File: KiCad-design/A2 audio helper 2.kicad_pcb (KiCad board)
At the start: 2 copper layers, 52 x 70 mm, 34 parts, among them J1 PIN HEADER 1x2, J10 PIN HEADER 1x4, J11 PIN HEADER 1x3, J12 PIN HEADER 1x3, J13 PIN HEADER 1x3, J2 PIN HEADER 1x2, J3 PIN HEADER 1x2, J4 PIN HEADER 1x2, J5 SJ1-3515N, J6 PIN HEADER 1x3, J7 PIN HEADER 1x3, J8 SJ1-3515N, J9 PIN HEADER 1x5, K1 SR11-5V-200-2C, SW2 SW_DPDT_x2, U1 pam8403

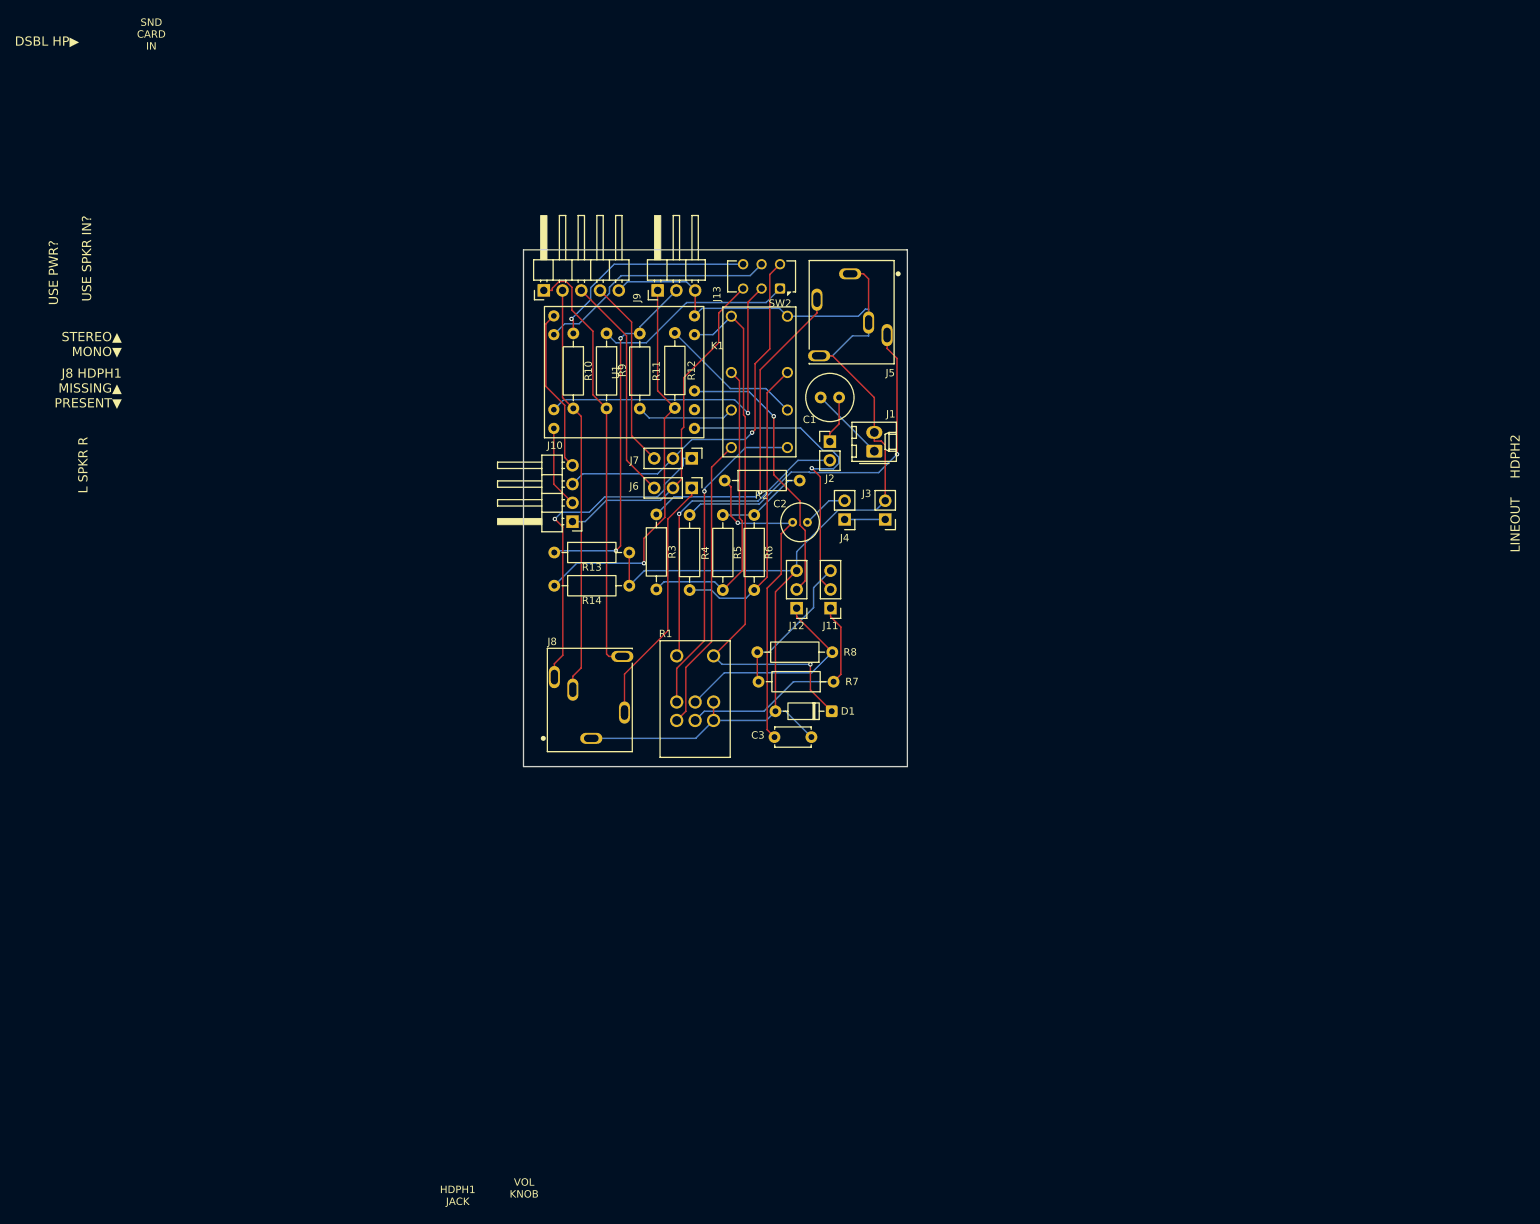
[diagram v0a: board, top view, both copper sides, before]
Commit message: minor simplification, 1st draft pcb
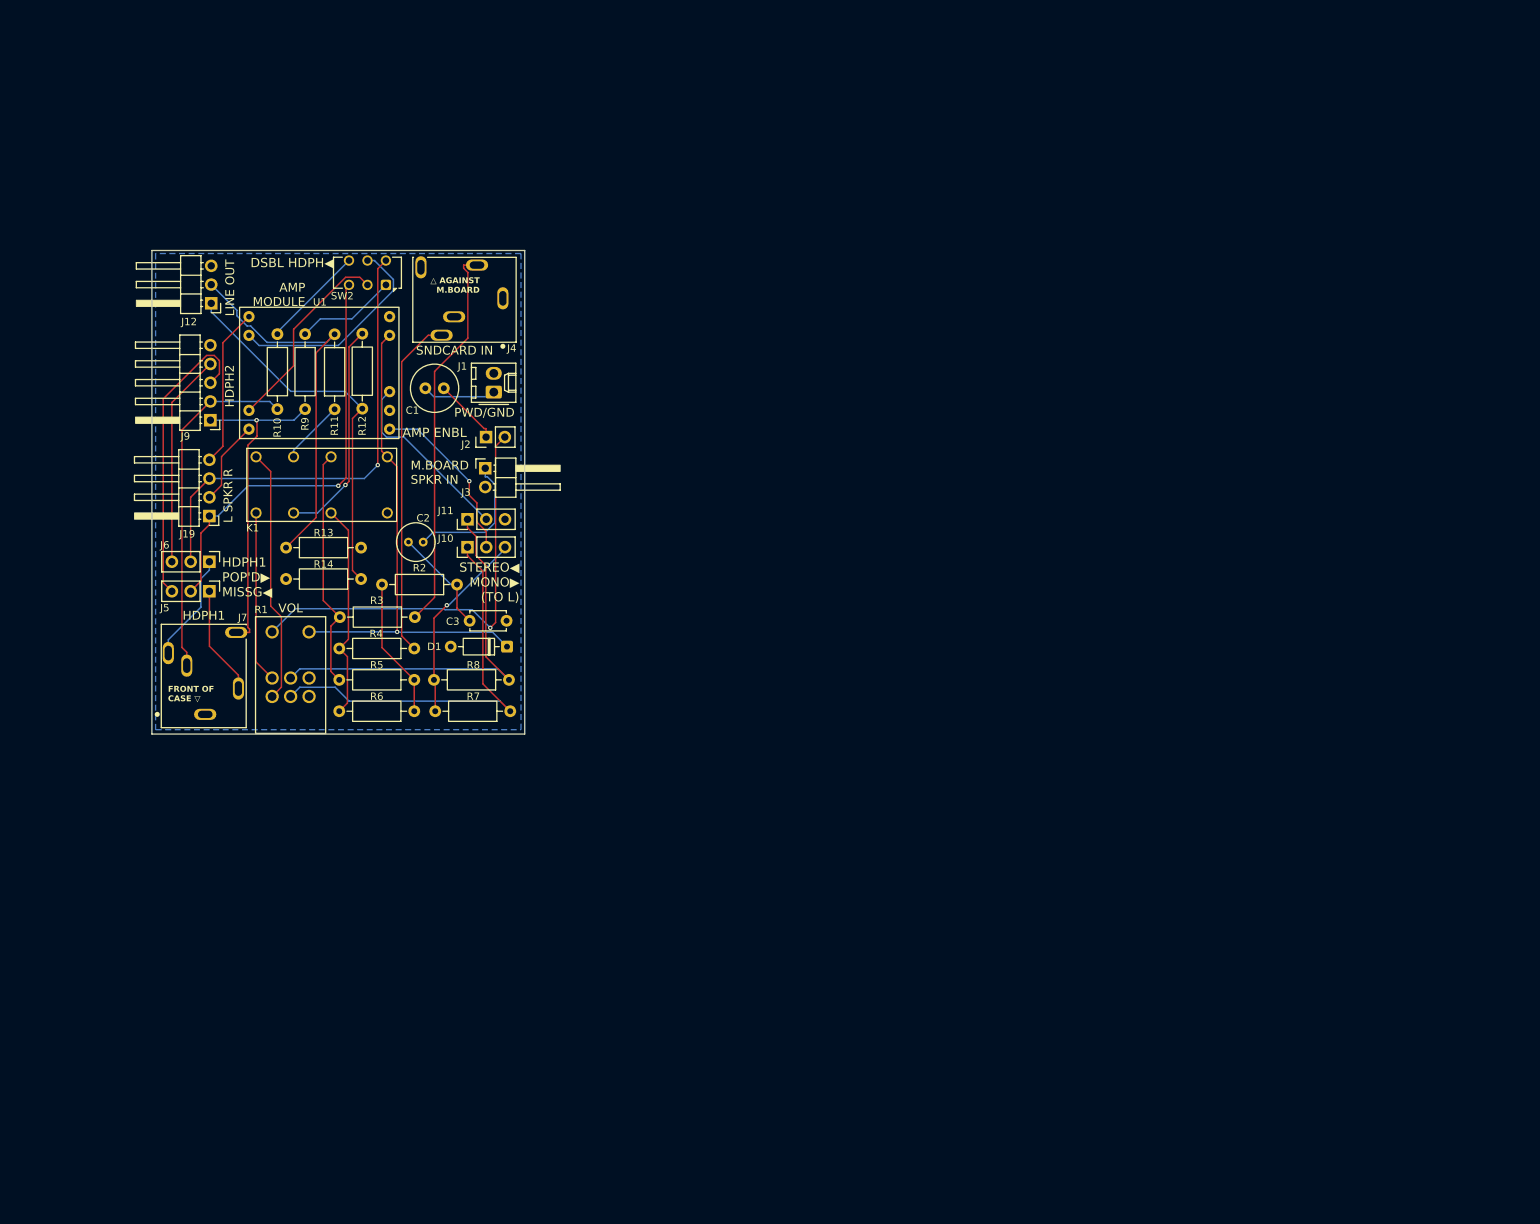
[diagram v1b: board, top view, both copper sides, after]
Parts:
- removed the J4 at (143.9, 86.5)
- J3: footprint Connector_PinHeader_2.54mm:PinHeader_1x02_P2.54mm_Vertical -> Connector_PinHeader_2.54mm:PinHeader_1x02_P2.54mm_Horizontal
- SW2: footprint Button_Switch_THT:SW_CK_JS202011AQN_DPDT_Angled -> Button_Switch_THT:SW_CK_JS202011CQN_DPDT_Straight
- moved J5 66.8 mm to (57.9, 96.2)
- moved J6 66.8 mm to (57.9, 92.2)
- moved K1 60.9 mm to (73.1, 81.8), turned to 0 degrees
- moved J12 60.5 mm to (58.1, 57.2), turned to 180 degrees
- moved R1 54.9 mm to (68.9, 108.0)
- moved J3 54.6 mm to (95.2, 79.6), turned to 0 degrees
- moved C1 53.6 mm to (87.1, 68.8)
- moved SW2 53.4 mm to (81.8, 54.8)
- moved R6 53.2 mm to (85.6, 112.5), turned to 180 degrees
- moved J7 52.4 mm to (57.3, 112.9)
- moved J1 52.2 mm to (96.4, 69.3)
- moved C2 52.1 mm to (86.8, 89.6)
- moved J10 49.9 mm to (92.8, 90.3), turned to 90 degrees
- moved J19 49.2 mm to (57.9, 86.1)
- moved J9 48.5 mm to (58.0, 73.1), turned to 180 degrees
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- renumbered J11 to J10, J12 to J11, J13 to J12, J10 to J19, J5 to J4, J6 to J5, J7 to J6, J8 to J7
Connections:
- C2 pad 1: Net-(J4-Pin_2) -> /MB_SPKR
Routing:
- net GND: track 185.7 -> 0.00 mm
- net /HP1_IS_PRIMARY_R: track 45.3 -> 14.7 mm, vias 1 -> 0
- net Net-(C2-Pad2): track 44.9 -> 14.6 mm, vias 1 -> 0
- net /VOLUME_ADJUSTED_R: track 29.3 -> 54.8 mm
- net /VOLUME_ADJUSTED_L: track 31.9 -> 56.2 mm
- net /VOLUME_SOURCE_R: track 44.0 -> 23.3 mm, vias 1 -> 0
- net /AMP_INPUT_L: track 43.5 -> 23.6 mm
- net /HP1_IS_PRIMARY_L: track 34.3 -> 14.8 mm
- net Net-(SW2A-B): track 45.2 -> 26.8 mm, vias 1 -> 0
- net /V_IN_ENABLED: track 42.8 -> 58.6 mm
- net Net-(SW2B-A): track 29.3 -> 14.0 mm, vias 1 -> 0
- net /HP_OUT_L: track 58.7 -> 44.6 mm, vias 0 -> 1
- net /MB_SPKR: track 5.50 -> 18.9 mm
- net Net-(SW2A-A): track 27.1 -> 13.7 mm
- net /AMP_INPUT_R: track 37.9 -> 25.0 mm, vias 1 -> 0
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- added copper zone on B.Cu, net GND
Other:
- board size 52 x 70 mm -> 50.5 x 65.5 mm
- board text added: "A2 Audio Helper v0.6"
- board text added: "AMP ENBL"
- board text added: "AMP MODULE"
- board text added: "DSBL HDPH◀︎"
- board text added: "FRONT OF CASE ▽"
- board text added: "HDPH1"
- board text added: "HDPH1 POP'D▶︎ MISSG◀︎"
- board text added: "LINE OUT"
- board text added: "M.BOARD SPKR IN"
- board text added: "Northwest Retroventures"
- board text added: "PWD/GND"
- board text added: "SNDCARD IN"
- board text added: "STEREO◀︎ MONO▶︎ (TO L)"
- board text added: "VOL"
- board text added: "△ AGAINST M.BOARD"
- board text removed: "DSBL HP▶︎"
- board text removed: "HDPH1 JACK"
- board text removed: "J8 HDPH1 MISSING▲ PRESENT▼"
- board text removed: "LINEOUT"
- board text removed: "SND CARD IN"
- board text removed: "STEREO▲ MONO▼"
- board text removed: "USE PWR?"
- board text removed: "USE SPKR IN?"
- board text removed: "VOL KNOB"

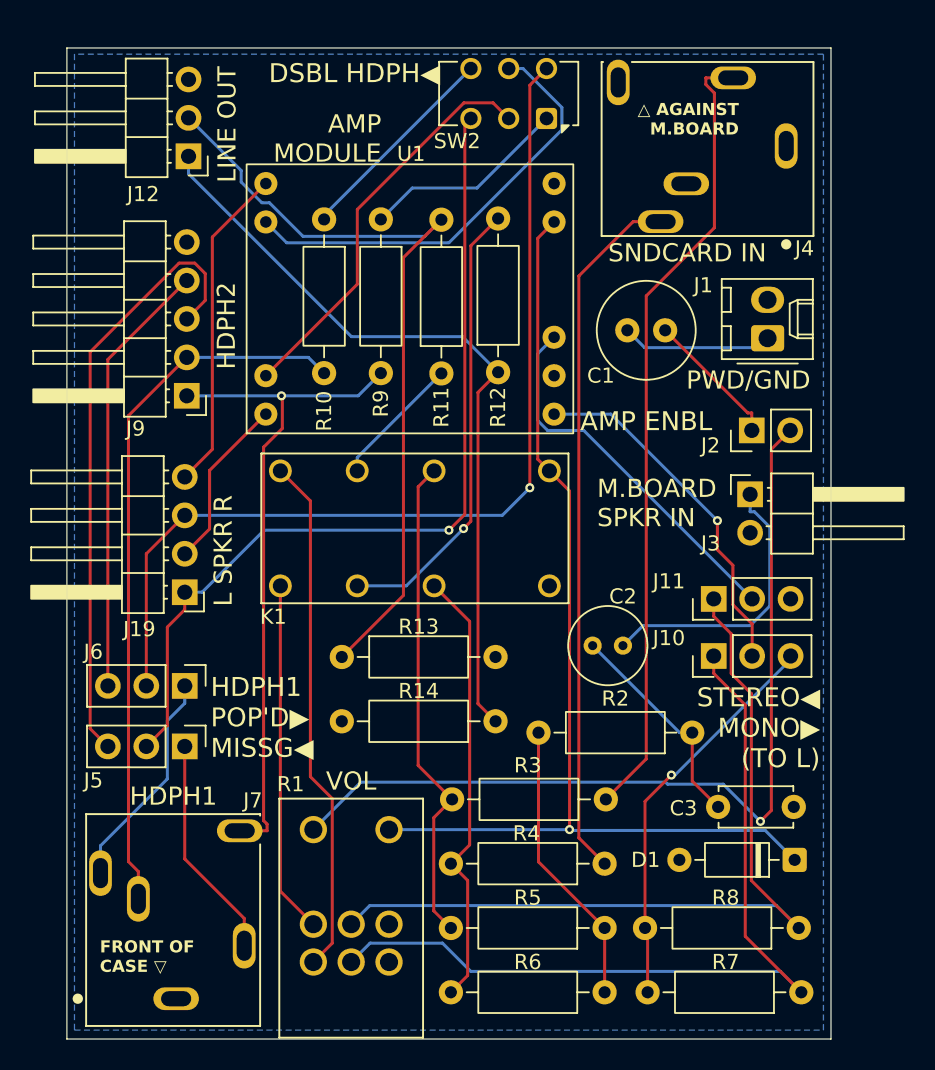
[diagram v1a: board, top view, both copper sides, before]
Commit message: picked new connectors, pcb take 2
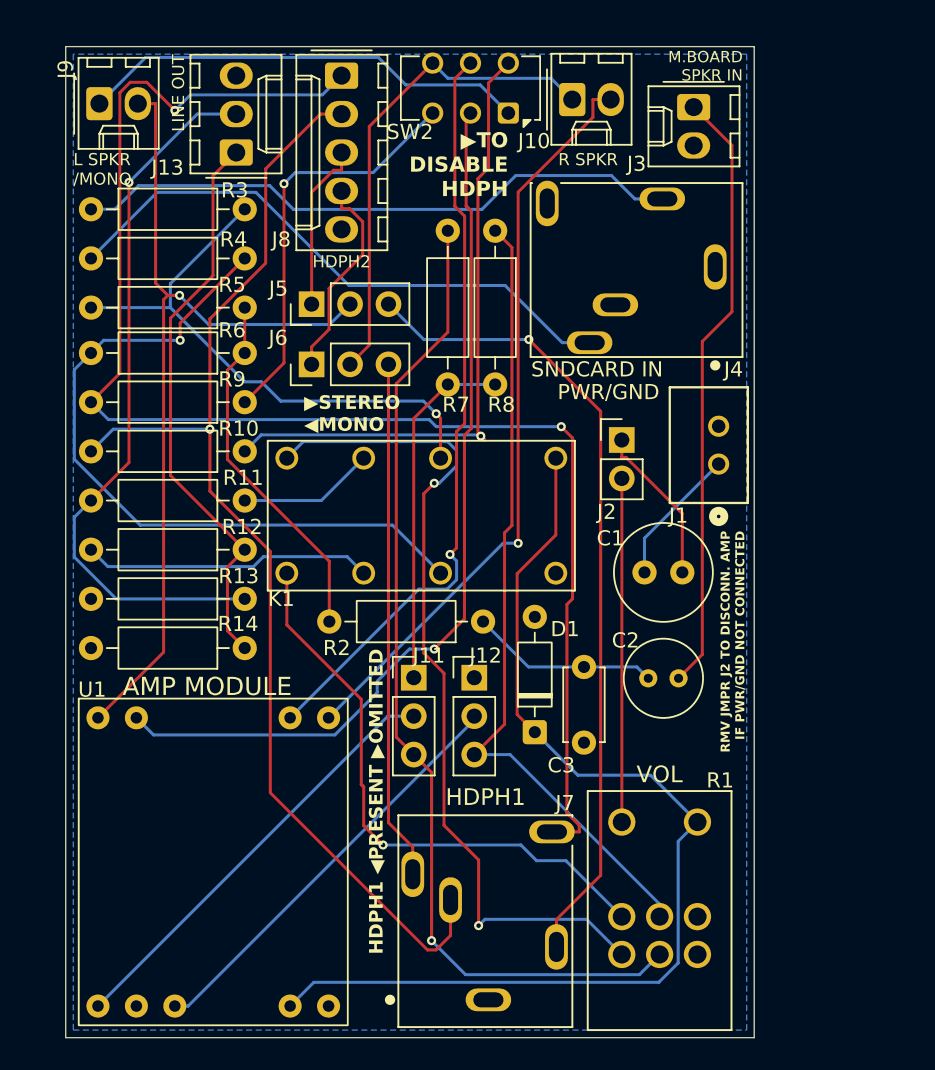
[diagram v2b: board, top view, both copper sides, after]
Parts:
- removed J19: PIN HEADER 1x4, Connector_PinHeader_2.54mm:PinHeader_1x04_P2.54mm_Horizontal
- added J10: PIN HEADER 1x2, Connector_Molex:Molex_KK-254_AE-6410-02A_1x02_P2.54mm_Vertical, F.Cu at (83.5, 53.5)
- added J9: PIN HEADER 1x2, Connector_Molex:Molex_KK-254_AE-6410-02A_1x02_P2.54mm_Vertical, F.Cu at (52.2, 53.8)
- J1: footprint Connector_Molex:Molex_KK-254_AE-6410-02A_1x02_P2.54mm_Vertical -> footprints:CONN_22035025_MOL
- J13: renamed from J12; footprint Connector_PinHeader_2.54mm:PinHeader_1x03_P2.54mm_Horizontal -> Connector_Molex:Molex_KK-254_AE-6410-03A_1x03_P2.54mm_Vertical
- J3: footprint Connector_PinHeader_2.54mm:PinHeader_1x02_P2.54mm_Horizontal -> Connector_Molex:Molex_KK-254_AE-6410-02A_1x02_P2.54mm_Vertical
- J8: renamed from J9; footprint Connector_PinHeader_2.54mm:PinHeader_1x05_P2.54mm_Horizontal -> Connector_Molex:Molex_KK-254_AE-6410-05A_1x05_P2.54mm_Vertical
- moved R7 55.5 mm to (75.2, 62.2), turned to -90 degrees
- moved R4 52.5 mm to (51.7, 64.0), turned to 0 degrees
- moved R3 51.8 mm to (51.7, 60.8), turned to 0 degrees
- moved R8 50.3 mm to (78.4, 62.2), turned to -90 degrees
- moved R6 48.5 mm to (61.8, 70.2)
- moved R5 47.4 mm to (61.8, 67.2)
- moved U1 38.6 mm to (59.8, 103.2), turned to 0 degrees
- moved J5 30.4 mm to (66.2, 67.0), turned to 90 degrees
- moved J3 25.9 mm to (91.5, 54.0), turned to -90 degrees
- moved J8 23.5 mm to (68.2, 51.9), turned to -90 degrees
- moved J6 22.8 mm to (66.2, 71.0), turned to 90 degrees
- moved J7 20.6 mm to (77.9, 113.0)
- moved R12 20.4 mm to (61.8, 83.2), turned to 180 degrees
- moved R1 20.4 mm to (89.2, 107.5)
- moved J11 19.9 mm to (73.0, 91.7), turned to 0 degrees
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- renumbered J10 to J11, J11 to J12
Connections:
- J11 pad 1: /VOLUME_ADJUSTED_L -> /MONO_MIX_POINT
- J11 pad 3: /MONO_MIX_POINT -> /VOLUME_ADJUSTED_L
- J12 pad 1: /VOLUME_ADJUSTED_R -> GND
- J12 pad 3: GND -> /VOLUME_ADJUSTED_R
- J5 pad 1: /HP1_IS_PRIMARY_L -> /HP2_IS_PRIMARY_L
- J5 pad 2: /LSPKR+ -> /LSPKR-
- J5 pad 3: /HP2_IS_PRIMARY_L -> /HP1_IS_PRIMARY_L
- J6 pad 1: /HP1_IS_PRIMARY_R -> /HP2_IS_PRIMARY_R
- J6 pad 3: /HP2_IS_PRIMARY_R -> /HP1_IS_PRIMARY_R
- R10 pad 1: Net-(SW2B-A) -> Net-(SW2B-C)
- R9 pad 1: Net-(SW2A-A) -> Net-(SW2A-C)
- SW2 pad 1: Net-(SW2A-A) -> /LSPKR+
- SW2 pad 3: /LSPKR+ -> Net-(SW2A-C)
- SW2 pad 4: Net-(SW2B-A) -> /RSPKR+
- SW2 pad 6: /RSPKR+ -> Net-(SW2B-C)
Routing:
- net /HP_OUT_L: track 44.6 -> 99.1 mm, vias 1 -> 2
- net /LSPKR-: track 11.5 -> 57.4 mm, vias 0 -> 1
- net Net-(SW2B-C): track 0.00 -> 43.1 mm, vias 0 -> 1
- net /HP1_IS_PRIMARY_L: track 14.8 -> 53.6 mm, vias 0 -> 1
- net /V_IN_ENABLED: track 58.6 -> 22.7 mm, vias 1 -> 0
- net Net-(SW2A-B): track 26.8 -> 59.9 mm, vias 0 -> 1
- net /RSPKR+: track 64.0 -> 32.4 mm, vias 1 -> 0
- net /HP_OUT_R: track 47.2 -> 78.3 mm, vias 0 -> 1
- net /HP2_IS_PRIMARY_L: track 40.4 -> 11.2 mm
- net /LSPKR+: track 58.2 -> 29.8 mm, vias 1 -> 0
- net /RSPKR-: track 21.6 -> 49.9 mm, vias 0 -> 1
- net Net-(SW2A-C): track 0.00 -> 27.3 mm, vias 0 -> 1
- net /VOLUME_SOURCE_L: track 34.4 -> 56.5 mm, vias 0 -> 2
- net /MB_SPKR: track 18.9 -> 40.3 mm
- net Net-(SW2B-B): track 29.3 -> 50.2 mm, vias 0 -> 1
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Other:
- board size 50.5 x 65.5 mm -> 45.5 x 65.5 mm
- board text added: "Apple 2 Audio Helper v0.7"
- board text added: "HDPH1 ◀︎PRESENT ▶︎OMITTED"
- board text added: "L SPKR /MONO"
- board text added: "PWR/GND"
- board text added: "R SPKR"
- board text added: "RMV JMPR J2 TO DISCONN. AMP IF PWR/GND NOT CONNECTED"
- board text added: "▶︎STEREO ◀︎MONO"
- board text added: "▶︎︎TO DISABLE HDPH"
- board text removed: "A2 Audio Helper v0.6"
- board text removed: "AMP ENBL"
- board text removed: "DSBL HDPH◀︎"
- board text removed: "FRONT OF CASE ▽"
- board text removed: "HDPH1 POP'D▶︎ MISSG◀︎"
- board text removed: "L SPKR R"
- board text removed: "PWD/GND"
- board text removed: "STEREO◀︎ MONO▶︎ (TO L)"
- board text removed: "△ AGAINST M.BOARD"
